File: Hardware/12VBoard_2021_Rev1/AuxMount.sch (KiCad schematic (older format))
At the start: 34 parts

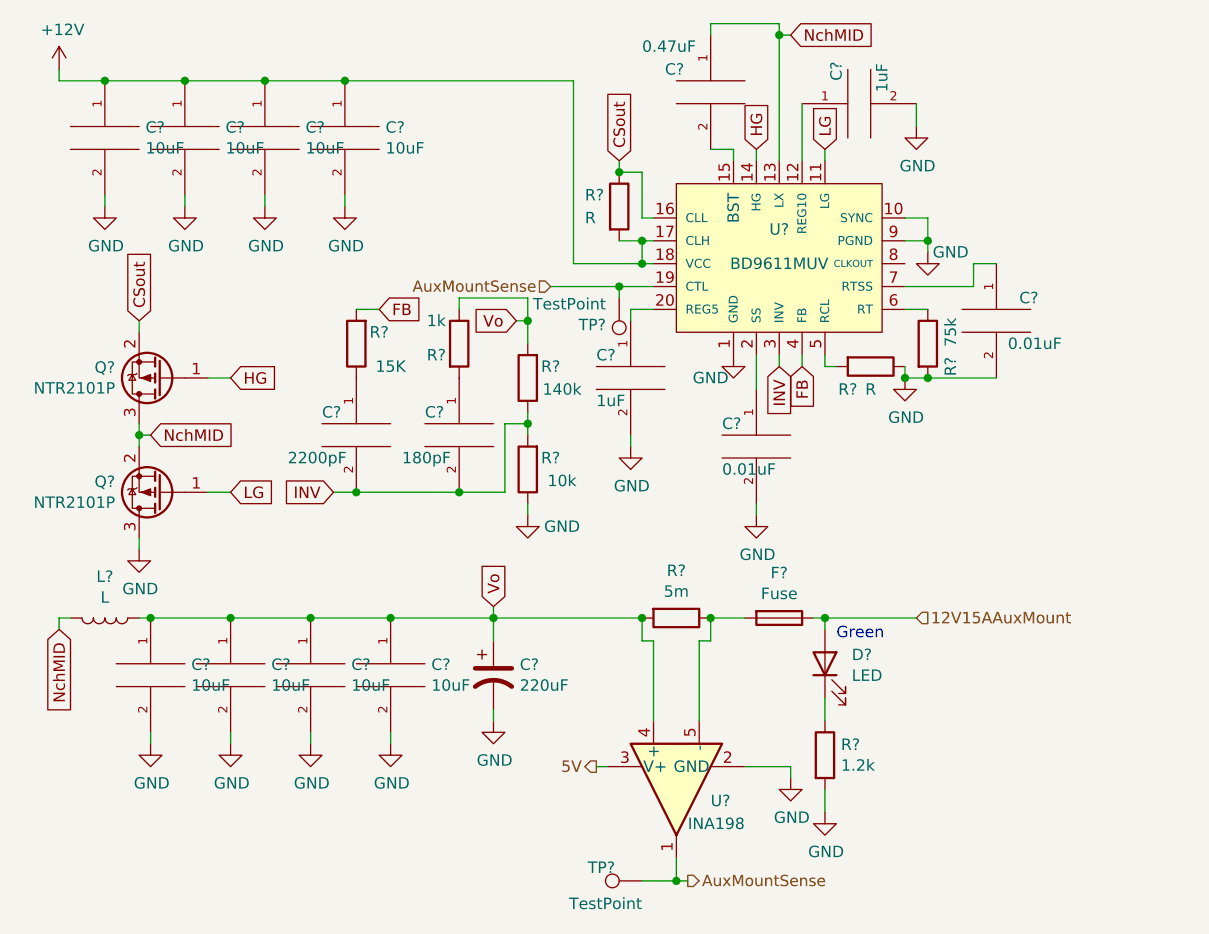
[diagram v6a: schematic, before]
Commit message: fixed High current for second review
addes gimbal to high current. added teva digital write pin to gimbal fot CTL. changed ports from 15 to 10 amp
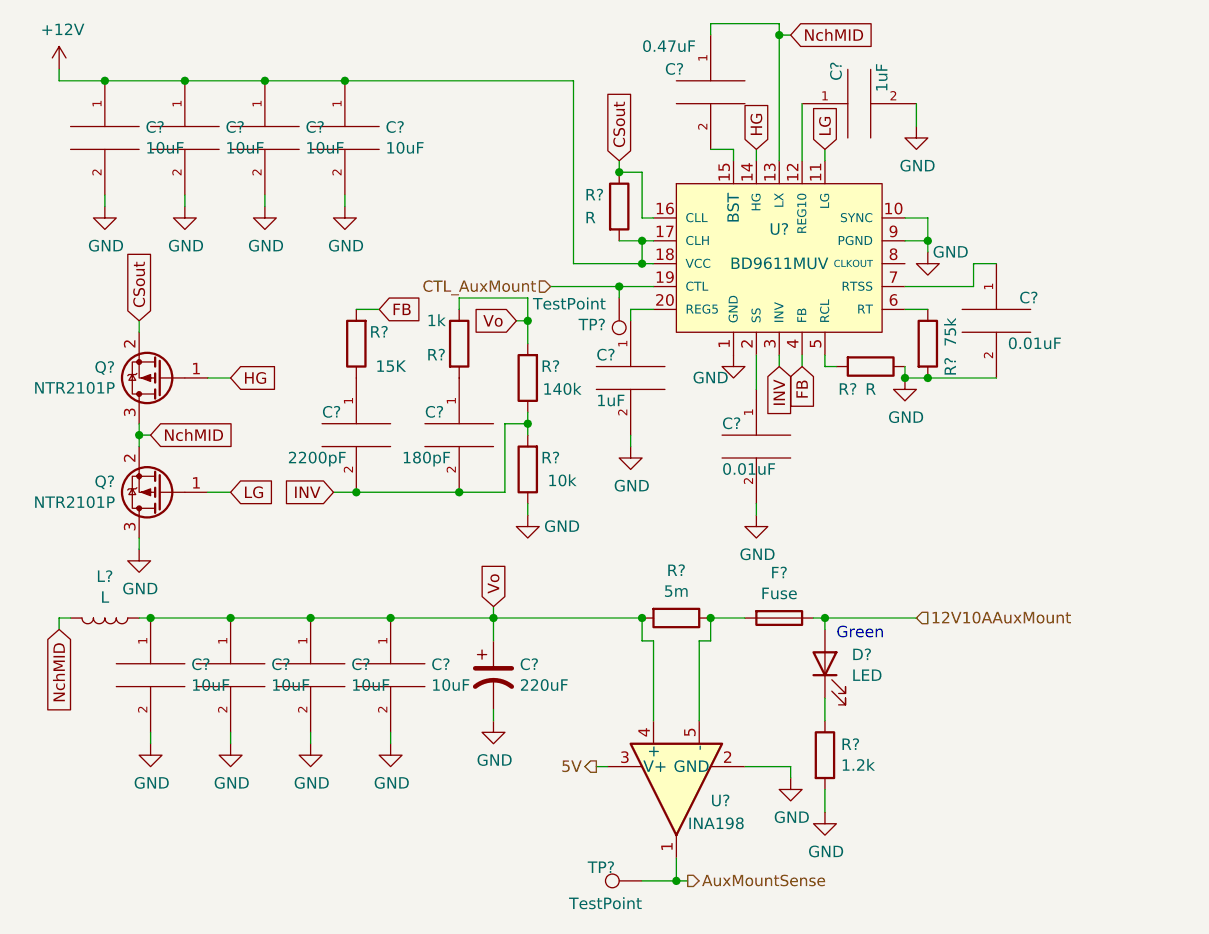
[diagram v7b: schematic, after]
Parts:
- removed C?: 2200pF, symbol pspice:CAP
- removed C?: 180pF, symbol pspice:CAP
- removed C?: 10uF, symbol pspice:CAP
- removed R?: 15K, symbol Device:R
- removed R?: 1k, symbol Device:R
- removed R?: R, symbol Device:R
- removed U?: BD9611MUV, symbol 12VBoard_2021_Rev1-rescue:BD9611MUV-12VBoard_2021_Rev1
- added C?: 2200pF, symbol pspice:CAP
- added C?: 180pF, symbol pspice:CAP
- added C?: 10uF, symbol pspice:CAP
- added R?: 15K, symbol Device:R
- added R?: 1k, symbol Device:R
- added R?: R, symbol Device:R
- added U?: BD9611MUV, symbol 12VBoard_2021_Rev1-rescue:BD9611MUV-12VBoard_2021_Rev1
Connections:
- net +12V: now also R?.2, U?.17 (CLH), U?.18 (VCC)
- net AuxMountSense: no longer TP?.1
- net CSout: now also R?.1, U?.16 (CLL)
- net FB: now also R?.2, U?.4 (FB)
- net GND: now also C?.2, U?.1 (GND), U?.10 (SYNC), U?.9 (PGND)
- net HG: now also U?.14 (HG)
- net INV: now also C?.2, C?.2, U?.3 (INV)
- net LG: now also U?.11 (LG)
- net NchMID: now also U?.13 (LX)
- net Vo: now also C?.1, R?.1
- net at C?.2: now also U?.15 (BST)
- net at C?.1: now also U?.20 (REG5)
- net at R?.2: now also U?.5 (RCL)
- net at C?.1: now also U?.2 (SS)
- net at C?.1: now also U?.12 (REG10)
- net at R?.1: now also U?.6 (RT)
- net at C?.1: now also U?.7 (RTSS)
- net 12V15AAuxMount renamed 12V10AAuxMount
- new net: C?.1, R?.1
- new net: C?.1, R?.2
- new net CTL_AuxMount: TP?.1, U?.19 (CTL)
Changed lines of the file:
@@
 $Descr A4 11693 8268
 encoding utf-8
-Sheet 7 7
+Sheet 7 8
 Title ""
 Date ""
@@
 $Comp
 L Device:R R?
-U 1 1 5F844392
+U 1 1 5F971E29
 P 2050 2000
-AR Path="/5F74F36B/5F844392" Ref="R?"  Part="1"
-AR Path="/5F74F36B/5F8222BE/5F844392" Ref="R?"  Part="1"
-AR Path="/5F74F36B/5F821EB2/5F844392" Ref="R?"  Part="1"
-AR Path="/5F74F36B/5F8236F9/5F844392" Ref="R?"  Part="1"
+AR Path="/5F74F36B/5F971E29" Ref="R?"  Part="1"
+AR Path="/5F74F36B/5F8222BE/5F971E29" Ref="R?"  Part="1"
+AR Path="/5F74F36B/5F821EB2/5F971E29" Ref="R?"  Part="1"
+AR Path="/5F74F36B/5F8236F9/5F971E29" Ref="R?"  Part="1"
 F 0 "R?" H 1950 1950 50  0000 C CNN
 F 1 "15K" H 1900 2100 50  0000 C CNN
@@
 $Comp
 L pspice:CAP C?
-U 1 1 5F844398
+U 1 1 5F971E2A
 P 2050 2400
-AR Path="/5F74F36B/5F844398" Ref="C?"  Part="1"
-AR Path="/5F74F36B/5F8222BE/5F844398" Ref="C?"  Part="1"
-AR Path="/5F74F36B/5F821EB2/5F844398" Ref="C?"  Part="1"
-AR Path="/5F74F36B/5F8236F9/5F844398" Ref="C?"  Part="1"
+AR Path="/5F74F36B/5F971E2A" Ref="C?"  Part="1"
+AR Path="/5F74F36B/5F8222BE/5F971E2A" Ref="C?"  Part="1"
+AR Path="/5F74F36B/5F821EB2/5F971E2A" Ref="C?"  Part="1"
+AR Path="/5F74F36B/5F8236F9/5F971E2A" Ref="C?"  Part="1"
 F 0 "C?" H 1900 2500 50  0000 L CNN
 F 1 "2200pF" H 1750 2300 50  0000 L CNN
@@
 $Comp
 L Device:R R?
-U 1 1 5F84439E
+U 1 1 5F971E2B
 P 2500 2000
-AR Path="/5F74F36B/5F84439E" Ref="R?"  Part="1"
-AR Path="/5F74F36B/5F8222BE/5F84439E" Ref="R?"  Part="1"
-AR Path="/5F74F36B/5F821EB2/5F84439E" Ref="R?"  Part="1"
-AR Path="/5F74F36B/5F8236F9/5F84439E" Ref="R?"  Part="1"
+AR Path="/5F74F36B/5F971E2B" Ref="R?"  Part="1"
+AR Path="/5F74F36B/5F8222BE/5F971E2B" Ref="R?"  Part="1"
+AR Path="/5F74F36B/5F821EB2/5F971E2B" Ref="R?"  Part="1"
+AR Path="/5F74F36B/5F8236F9/5F971E2B" Ref="R?"  Part="1"
 F 0 "R?" H 2400 1950 50  0000 C CNN
 F 1 "1k" H 2400 2100 50  0000 C CNN
@@
 $Comp
 L pspice:CAP C?
-U 1 1 5F8443A4
+U 1 1 5F971E2C
 P 2500 2400
-AR Path="/5F74F36B/5F8443A4" Ref="C?"  Part="1"
-AR Path="/5F74F36B/5F8222BE/5F8443A4" Ref="C?"  Part="1"
-AR Path="/5F74F36B/5F821EB2/5F8443A4" Ref="C?"  Part="1"
-AR Path="/5F74F36B/5F8236F9/5F8443A4" Ref="C?"  Part="1"
+AR Path="/5F74F36B/5F971E2C" Ref="C?"  Part="1"
+AR Path="/5F74F36B/5F8222BE/5F971E2C" Ref="C?"  Part="1"
+AR Path="/5F74F36B/5F821EB2/5F971E2C" Ref="C?"  Part="1"
+AR Path="/5F74F36B/5F8236F9/5F971E2C" Ref="C?"  Part="1"
 F 0 "C?" H 2350 2500 50  0000 L CNN
 F 1 "180pF" H 2250 2300 50  0000 L CNN
@@
 $Comp
 L 12VBoard_2021_Rev1-rescue:BD9611MUV-12VBoard_2021_Rev1 U?
-U 1 1 5F8443B4
+U 1 1 5F971E2D
 P 3900 1650
-AR Path="/5F8443B4" Ref="U?"  Part="1"
-AR Path="/5F74F36B/5F8443B4" Ref="U?"  Part="1"
-AR Path="/5F74F36B/5F8222BE/5F8443B4" Ref="U?"  Part="1"
-AR Path="/5F74F36B/5F821EB2/5F8443B4" Ref="U?"  Part="1"
-AR Path="/5F74F36B/5F8236F9/5F8443B4" Ref="U?"  Part="1"
+AR Path="/5F971E2D" Ref="U?"  Part="1"
+AR Path="/5F74F36B/5F971E2D" Ref="U?"  Part="1"
+AR Path="/5F74F36B/5F8222BE/5F971E2D" Ref="U?"  Part="1"
+AR Path="/5F74F36B/5F821EB2/5F971E2D" Ref="U?"  Part="1"
+AR Path="/5F74F36B/5F8236F9/5F971E2D" Ref="U?"  Part="1"
 F 0 "U?" H 3900 1800 50  0000 C CNN
 F 1 "BD9611MUV" H 3900 1650 50  0000 C CNN
@@
 $Comp
 L Device:R R?
-U 1 1 5F8443C6
+U 1 1 5F971E2E
 P 3200 1400
-AR Path="/5F74F36B/5F8443C6" Ref="R?"  Part="1"
-AR Path="/5F74F36B/5F8222BE/5F8443C6" Ref="R?"  Part="1"
-AR Path="/5F74F36B/5F821EB2/5F8443C6" Ref="R?"  Part="1"
-AR Path="/5F74F36B/5F8236F9/5F8443C6" Ref="R?"  Part="1"
+AR Path="/5F74F36B/5F971E2E" Ref="R?"  Part="1"
+AR Path="/5F74F36B/5F8222BE/5F971E2E" Ref="R?"  Part="1"
+AR Path="/5F74F36B/5F821EB2/5F971E2E" Ref="R?"  Part="1"
+AR Path="/5F74F36B/5F8236F9/5F971E2E" Ref="R?"  Part="1"
 F 0 "R?" H 3050 1450 50  0000 L CNN
 F 1 "R" H 3050 1350 50  0000 L CNN
@@
 $Comp
 L pspice:CAP C?
-U 1 1 5F844406
+U 1 1 5F971E2F
 P 1500 3450
-AR Path="/5F74F36B/5F844406" Ref="C?"  Part="1"
-AR Path="/5F74F36B/5F8222BE/5F844406" Ref="C?"  Part="1"
-AR Path="/5F74F36B/5F821EB2/5F844406" Ref="C?"  Part="1"
-AR Path="/5F74F36B/5F8236F9/5F844406" Ref="C?"  Part="1"
+AR Path="/5F74F36B/5F971E2F" Ref="C?"  Part="1"
+AR Path="/5F74F36B/5F8222BE/5F971E2F" Ref="C?"  Part="1"
+AR Path="/5F74F36B/5F821EB2/5F971E2F" Ref="C?"  Part="1"
+AR Path="/5F74F36B/5F8236F9/5F971E2F" Ref="C?"  Part="1"
 F 0 "C?" H 1678 3496 50  0000 L CNN
 F 1 "10uF" H 1678 3405 50  0000 L CNN
@@
 $Comp
 L power:GND #PWR?
-U 1 1 5F844412
+U 1 1 5F971E31
 P 1150 3750
-AR Path="/5F74F36B/5F844412" Ref="#PWR?"  Part="1"
-AR Path="/5F74F36B/5F8222BE/5F844412" Ref="#PWR?"  Part="1"
-AR Path="/5F74F36B/5F821EB2/5F844412" Ref="#PWR?"  Part="1"
-AR Path="/5F74F36B/5F8236F9/5F844412" Ref="#PWR?"  Part="1"
+AR Path="/5F74F36B/5F971E31" Ref="#PWR?"  Part="1"
+AR Path="/5F74F36B/5F8222BE/5F971E31" Ref="#PWR?"  Part="1"
+AR Path="/5F74F36B/5F821EB2/5F971E31" Ref="#PWR?"  Part="1"
+AR Path="/5F74F36B/5F8236F9/5F971E31" Ref="#PWR?"  Part="1"
 F 0 "#PWR?" H 1150 3500 50  0001 C CNN
 F 1 "GND" H 1155 3577 50  0000 C CNN
@@
 $Comp
 L power:GND #PWR?
-U 1 1 5F844418
+U 1 1 5F971E32
 P 1500 3750
-AR Path="/5F74F36B/5F844418" Ref="#PWR?"  Part="1"
-AR Path="/5F74F36B/5F8222BE/5F844418" Ref="#PWR?"  Part="1"
-AR Path="/5F74F36B/5F821EB2/5F844418" Ref="#PWR?"  Part="1"
-AR Path="/5F74F36B/5F8236F9/5F844418" Ref="#PWR?"  Part="1"
+AR Path="/5F74F36B/5F971E32" Ref="#PWR?"  Part="1"
+AR Path="/5F74F36B/5F8222BE/5F971E32" Ref="#PWR?"  Part="1"
+AR Path="/5F74F36B/5F821EB2/5F971E32" Ref="#PWR?"  Part="1"
+AR Path="/5F74F36B/5F8236F9/5F971E32" Ref="#PWR?"  Part="1"
 F 0 "#PWR?" H 1500 3500 50  0001 C CNN
 F 1 "GND" H 1505 3577 50  0000 C CNN
@@
 $Comp
 L power:GND #PWR?
-U 1 1 5F844424
+U 1 1 5F971E33
 P 2200 3750
-AR Path="/5F74F36B/5F844424" Ref="#PWR?"  Part="1"
-AR Path="/5F74F36B/5F8222BE/5F844424" Ref="#PWR?"  Part="1"
-AR Path="/5F74F36B/5F821EB2/5F844424" Ref="#PWR?"  Part="1"
-AR Path="/5F74F36B/5F8236F9/5F844424" Ref="#PWR?"  Part="1"
+AR Path="/5F74F36B/5F971E33" Ref="#PWR?"  Part="1"
+AR Path="/5F74F36B/5F8222BE/5F971E33" Ref="#PWR?"  Part="1"
+AR Path="/5F74F36B/5F821EB2/5F971E33" Ref="#PWR?"  Part="1"
+AR Path="/5F74F36B/5F8236F9/5F971E33" Ref="#PWR?"  Part="1"
 F 0 "#PWR?" H 2200 3500 50  0001 C CNN
 F 1 "GND" H 2205 3577 50  0000 C CNN
@@
 5V
 Text HLabel 4500 3200 2    50   Input ~ 0
-12V15AAuxMount
+12V10AAuxMount
 Text HLabel 3500 4350 2    49   Output ~ 0
 AuxMountSense
@@
 	3450 4350 3500 4350
 Text HLabel 2900 1750 0    49   Input ~ 0
-AuxMountSense
+CTL_AuxMount
 $Comp
 L Connector:TestPoint TP?

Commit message: fixed some stuffs
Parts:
- D14: renamed from D?; footprint (none) -> Diode_SMD:D_0603_1608Metric_Pad1.05x0.95mm_HandSolder
- F2: renamed from F?; value Fuse -> 10AMP
- TP7, TP8: renamed from TP?; footprint (none) -> TestPoint:TestPoint_Pad_2.5x2.5mm
- gave numbers to parts that had none: 30
